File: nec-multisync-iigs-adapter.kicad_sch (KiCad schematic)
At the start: 2 parts, among them J1 DA15_Plug

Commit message: V1 to Fab
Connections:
- net GND: now also J2.11, J2.4; no longer J1.1, J1.13 (P13), J1.6, J2.6, J2.7, J2.8
- new net Blue_GND: J1.13 (P13), J2.8
- new net Green_GND: J1.6, J2.7
- new net Red_GND: J1.1, J2.6
- no-connect marks 14 -> 12
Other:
- note added: "from https://stason.org/TULARC/pc/apple2/faq/16-015-Which-monitors-and-adapters-can-I-use-to-replace-my-I.html (modified for MultiSync 3D)"
- note added: "to NEC MultiSync - Female"
- note removed: "TODO: Maybe add a CSync splitter but who cares"
- note removed: "to NEC MultiSync"
- moved on the sheet: J2

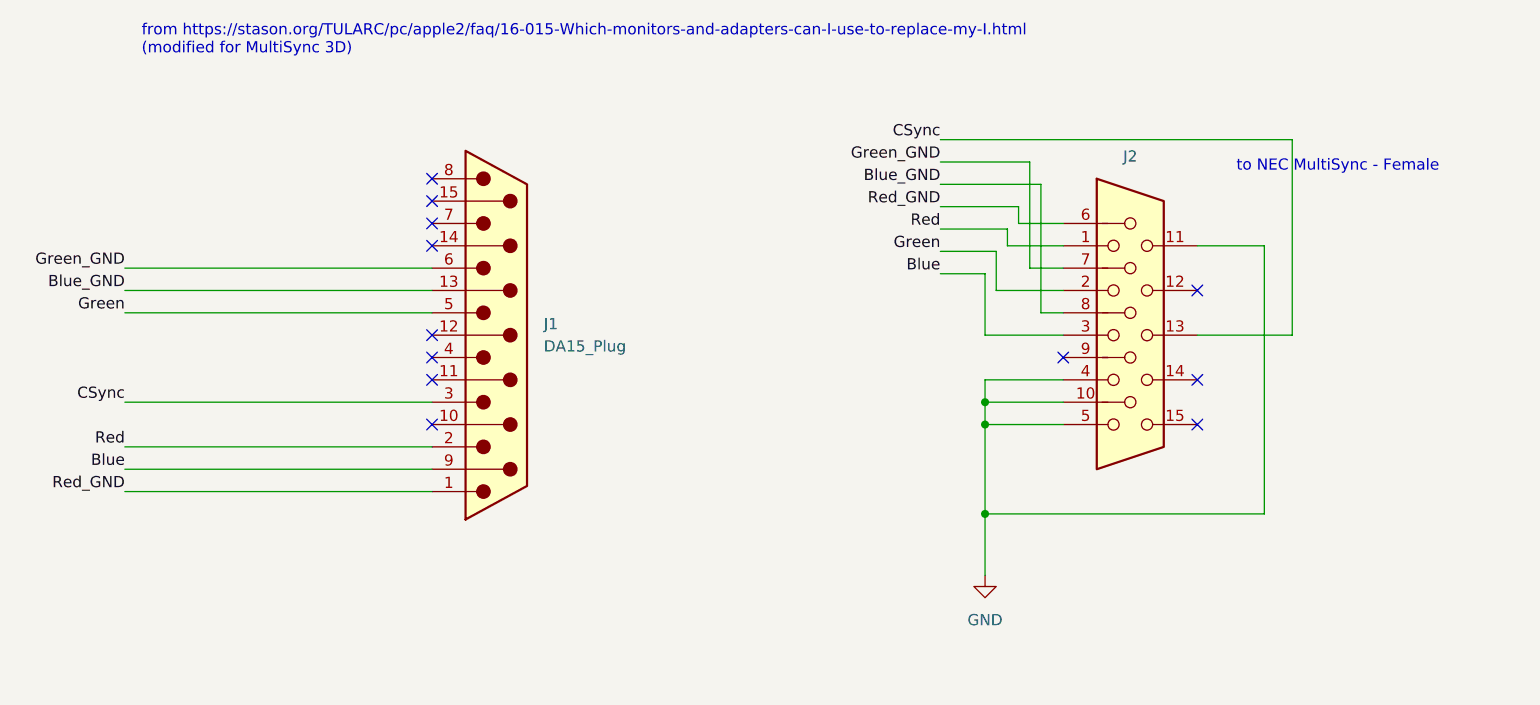
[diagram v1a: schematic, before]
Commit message: Tie shields together; MultiSync now works
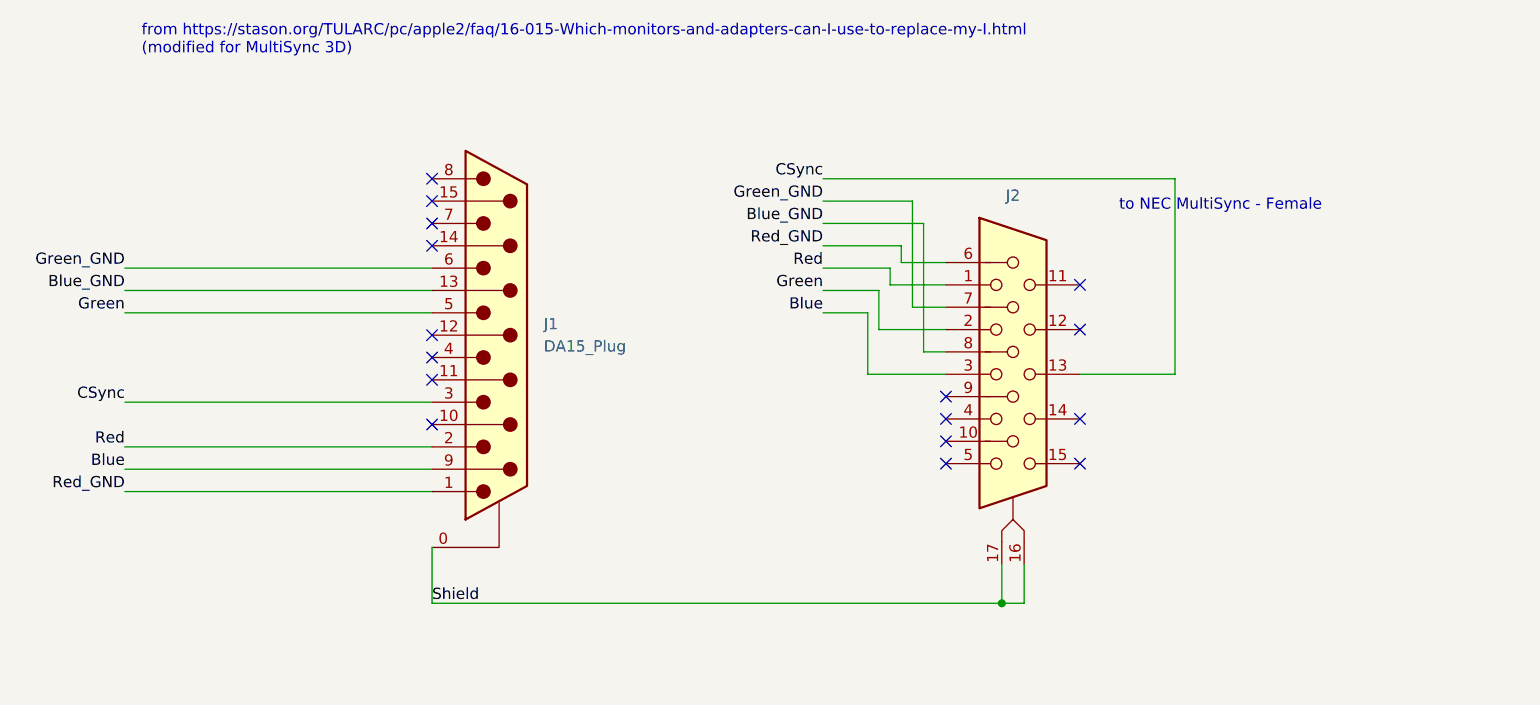
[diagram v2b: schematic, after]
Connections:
- removed net GND: J2.10, J2.11, J2.4, J2.5
- new net Shield: J1.0 (Shield), J2.16 (Shield_1), J2.17 (Shield_1)
- no-connect marks 12 -> 16

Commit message: README with parts
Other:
- note removed: "from https://stason.org/TULARC/pc/apple2/faq/16-015-Which-monitors-and-adapters-can-I-use-to-replace-my-I.html (modified for MultiSync 3D)"
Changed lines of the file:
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@@
     (stroke (width 0) (type default))
-  )
-  (text "from https://stason.org/TULARC/pc/apple2/faq/16-015-Which-monitors-and-adapters-can-I-use-to-replace-my-I.html\n(modified for MultiSync 3D)"
-    (at 44.45 56.515 0)
-    (effects (font (size 1.27 1.27)) (justify left bottom))
   )
   (text "to NEC MultiSync - Female" (at 155.575 74.295 0)
